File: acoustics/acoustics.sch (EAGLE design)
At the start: 172 parts, among them J1 22-27-2021-02, J2 22-27-2021-02, J3 22-27-2021-02, J4 22-27-2021-02, X1 22-23-2021, X2 22-23-2021, X3 22-23-2021, X4 22-23-2021

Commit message: One channel done-ish for 4/5 meeting with Dave
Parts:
- removed C15, C16, C17, C19, C20, C21, C49: 1uf, rcl:C-EUC0805K
- removed C50: 10uf, rcl:C-EUC0805K
- removed C51: 0.1uf, rcl:C-EUC0805K
- removed C52: 47uf, rcl:C-EUC0805K
- removed R5: 60.4k, rcl:R-US_M0805
- removed R6: 10K, rcl:R-US_M0805
- added H4ADC_C: 1uf, rcl:C-EUC0603K
- added H4RF_C_4, H4_C1, H4_C11, H4_C2, H4_C25, H4_C_POW: 1uf, rcl:C-EUC0603
- added H4RF_C_IN: 10uf, rcl:C-EUC0603
- added H4RF_C_O1: 47uf, rcl:C-EUC0603
- added H4RF_C_O2: 0.1uf, rcl:C-EUC0603
- added H4_R6: 10K, rcl:R-US_R0603
- added H4_R7: 60.4k, rcl:R-US_R0603
- renumbered C63 to HFPA_C, C64 to HFPA_C_INP, C65 to HFPA_C_FB, C66 to H4PA_C_IN, C67 to H4DA_C_OFN, C68 to H4DA_C_OFP, C69 to H4DA_CI2, C70 to H4DA_CI1, C72 to H4DA_C_O, J1 to H1CON, J2 to H2CON, J3 to H3CON, J4 to H4_OUT, R49 to HFPA_R_FB, R50 to HFPA_R, R51 to HFPA_R2, R52 to HFPA_R_IN, R53 to H4DA_R_IP2, R54 to H4DA_R_IP1, R55 to H4DA_R_IN1, R56 to H4DA_R_IN2, R57 to H4DA_R_ON1, R58 to H4DA_R_OP1, R59 to H4DA_R_OFN, R60 to H4DA_R_OFP, R63 to H4DA_R_ON2, R64 to H4DA_R_OP2, R69 to H4RF_R_3, R70 to H4RF_R_0, U$12 to H4_REFGEN, U$8 to H4_DIFAMP, U$9 to H4_PREAMP, X4 to H4_IN
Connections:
- net N$6 renamed START
- new net H4_REFV: ADC_H4.REFP, H4RF_C_O1.2, H4RF_C_O2.2, H4_REFGEN.OUT_F, H4_REFGEN.OUT_S
- net +3V3: now also H4ADC_C.1, H4RF_C_IN.2, H4_C_POW.1; no longer C17.1, C20.1, C50.2
- net AGND: now also H4ADC_C.2, H4RF_C_4.1, H4RF_C_IN.1, H4RF_C_O2.1, H4_C1.1, H4_C11.2, H4_C2.1, H4_R6.2, H4_R7.2; no longer C15.1, C16.1, C17.2, C19.2, C49.1, C50.1, C51.1, R5.2, R6.2
- net GND: now also ADC_H4.FILTER0, ADC_H4.FILTER1, ADC_H4.FSMODE, H4_C25.1, H4_C_POW.2; no longer C20.2, C21.1
- net N$11: now also H4_C1.2; no longer C16.2
- net N$24: now also H4_C2.2; no longer C15.2
- net N$31: now also H4_R6.1; no longer R6.1
- net N$32: now also H4_R7.1; no longer R5.1
- net N$35: now also H4_C11.1; no longer C19.1
- net N$38: now also H4_C25.2; no longer C21.2
- net N$83: now also H4RF_C_4.2; no longer C49.2
- net N$85: now also H4RF_C_O1.1; no longer C52.1
- net POSITIVE_REF: no longer ADC_H4.REFP, C51.2, C52.2, H4_REFGEN.OUT_F, H4_REFGEN.OUT_S

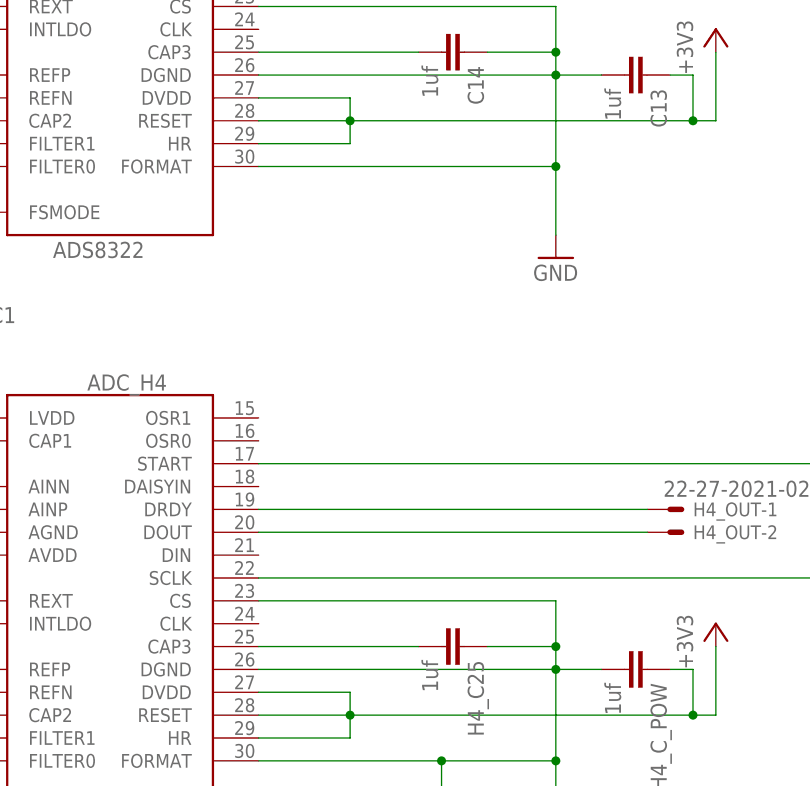
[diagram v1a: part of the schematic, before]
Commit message: One channel done updated Dave's suggestions
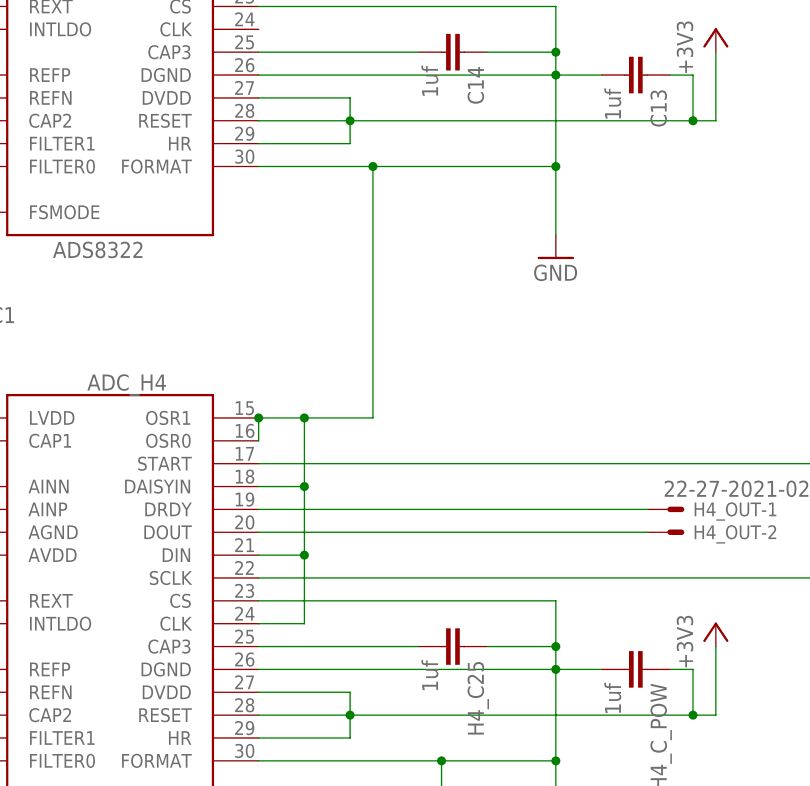
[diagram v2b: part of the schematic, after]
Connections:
- net GND: now also ADC_H4.CLK, ADC_H4.DAISYIN, ADC_H4.DIN, ADC_H4.OSR0, ADC_H4.OSR1
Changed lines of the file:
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@@
 <wire x1="269.24" y1="-71.12" x2="269.24" y2="-81.28" width="0.1524" layer="91"/>
 <wire x1="269.24" y1="-81.28" x2="269.24" y2="-88.9" width="0.1524" layer="91"/>
-<wire x1="236.22" y1="-81.28" x2="269.24" y2="-81.28" width="0.1524" layer="91"/>
+<wire x1="236.22" y1="-81.28" x2="248.92" y2="-81.28" width="0.1524" layer="91"/>
 <junction x="269.24" y="-81.28"/>
 <pinref part="GND2" gate="1" pin="GND"/>
 <pinref part="C14" gate="G$1" pin="1"/>
+<wire x1="248.92" y1="-81.28" x2="269.24" y2="-81.28" width="0.1524" layer="91"/>
 <wire x1="261.62" y1="-68.58" x2="269.24" y2="-68.58" width="0.1524" layer="91"/>
 <junction x="269.24" y="-68.58"/>
@@
 <pinref part="C13" gate="G$1" pin="2"/>
 <wire x1="274.32" y1="-71.12" x2="269.24" y2="-71.12" width="0.1524" layer="91"/>
+<pinref part="ADC_H4" gate="G$1" pin="OSR1"/>
+<pinref part="ADC_H4" gate="G$1" pin="OSR0"/>
+<wire x1="236.22" y1="-109.22" x2="236.22" y2="-111.76" width="0.1524" layer="91"/>
+<wire x1="236.22" y1="-109.22" x2="241.3" y2="-109.22" width="0.1524" layer="91"/>
+<wire x1="241.3" y1="-109.22" x2="248.92" y2="-109.22" width="0.1524" layer="91"/>
+<wire x1="248.92" y1="-109.22" x2="248.92" y2="-81.28" width="0.1524" layer="91"/>
+<junction x="236.22" y="-109.22"/>
+<junction x="248.92" y="-81.28"/>
+<pinref part="ADC_H4" gate="G$1" pin="DAISYIN"/>
+<wire x1="236.22" y1="-116.84" x2="241.3" y2="-116.84" width="0.1524" layer="91"/>
+<wire x1="241.3" y1="-116.84" x2="241.3" y2="-109.22" width="0.1524" layer="91"/>
+<junction x="241.3" y="-109.22"/>
+<pinref part="ADC_H4" gate="G$1" pin="DIN"/>
+<wire x1="236.22" y1="-124.46" x2="241.3" y2="-124.46" width="0.1524" layer="91"/>
+<wire x1="241.3" y1="-124.46" x2="241.3" y2="-116.84" width="0.1524" layer="91"/>
+<junction x="241.3" y="-116.84"/>
+<pinref part="ADC_H4" gate="G$1" pin="CLK"/>
+<wire x1="236.22" y1="-132.08" x2="241.3" y2="-132.08" width="0.1524" layer="91"/>
+<wire x1="241.3" y1="-132.08" x2="241.3" y2="-124.46" width="0.1524" layer="91"/>
+<junction x="241.3" y="-124.46"/>
 </segment>
 </net>

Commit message: Combining AGND and GND into one
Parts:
- removed C1, C10, C11, C12, C13, C14, C2, C3, C4, C47, C5, C6, C7, C9: 1uf, rcl:C-EUC0805K
- removed C48, C8: 10uf, rcl:C-EUC0805K
- removed C74, C76: 0.1uf, rcl:C-EUC0805K
- removed C75, C77: 47uf, rcl:C-EUC0805K
- removed R1, R2: 60.4k, rcl:R-US_M0805
- removed R3, R4: 10K, rcl:R-US_M0805
- added H2ADC_C9, H3ADC_C9: 0.1uf, rcl:C-EUC0603
- added H2RF_C1, H3RF_C1: 10uf, rcl:C-EUC0603
- added H2RF_C4, H2_C1, H2_C11, H2_C2, H2_C25, H2_C27, H2_C6, H3RF_C4, H3_ADC_C5, H3_C1, H3_C11, H3_C2, H3_C25, H3_C27: 1uf, rcl:C-EUC0603
- added H2RF_C6, H3RF_C6: 47uf, rcl:C-EUC0603
- added H2_R7, H3_R7: 60.4k, rcl:R-US_R0603
- added H2_R8, H3_R8: 10K, rcl:R-US_R0603
- renumbered R67 to H2RF_R3, R68 to H3RF_R3, R71 to H2RF_RO, R72 to H3RF_RO
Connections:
- new net N$37: ADC_H3.REFP, H3ADC_C9.2, H3RF_C6.2, U$11.OUT_F, U$11.OUT_S
- new net N$6: ADC_H1.REFP, C25.2, C73.2, U$1.OUT_F, U$1.OUT_S
- net +3V3: now also H2RF_C1.2, H2_C27.1, H2_C6.2, H3RF_C1.2, H3_ADC_C5.1, H3_C27.1; no longer C10.1, C11.2, C12.1, C13.1, C48.2, C8.2
- net AGND: no longer ADC_H1.AGND, ADC_H1.REFN, ADC_H2.AGND, ADC_H2.REFN, ADC_H3.AGND, ADC_H3.REFN, ADC_H4.AGND, ADC_H4.REFN, C1.1, C10.2, C11.1, C2.1, C22.1, C23.1, C24.2, C25.1, C26.2, C29.1, C3.1, C30.1, C31.1, C39.1, C4.2, C41.2, C47.1, C48.1, C54.1, C55.2, C6.1, C7.1, C74.1, C76.1, C8.1, C9.2, H2RF_R3.1, H2RF_RO.1, H3RF_R3.1, H3RF_RO.1, H4ADC_C.2, H4DA_R_IN1.1, H4RF_C_4.1, H4RF_C_IN.1, H4RF_C_O2.1, H4RF_R_0.1, H4RF_R_3.1, H4_C1.1, H4_C11.2, H4_C2.1, H4_DIFAMP.VS-, H4_IN-1.S, H4_PREAMP.V-, H4_R6.2, H4_R7.2, H4_REFGEN.GND_F, H4_REFGEN.GND_S, HFPA_C.1, HFPA_C_INP.2, HFPA_R.2, R1.2, R15.1, R2.2, R24.2, R29.1, R3.2, R36.2, R4.2, R41.1, R65.1, R66.1, R7.2, R8.2, U$1.GND_F, U$1.GND_S, U$10.GND_F, U$10.GND_S, U$11.GND_F, U$11.GND_S, U$2.VS-, U$3.VS-, U$4.V-, U$5.VS-, U$6.V-, U$7.V-, X1-1.S, X2-1.S, X3-1.S
- net GND: now also ADC_H1.AGND, ADC_H1.REFN, ADC_H2.AGND, ADC_H2.DAISYIN, ADC_H2.DIN, ADC_H2.FILTER0, ADC_H2.FILTER1, ADC_H2.FSMODE, ADC_H2.OSR0, ADC_H2.OSR1, ADC_H2.REFN, ADC_H3.AGND, ADC_H3.DAISYIN, ADC_H3.DIN, ADC_H3.FILTER0, ADC_H3.FILTER1, ADC_H3.FSMODE, ADC_H3.OSR0, ADC_H3.OSR1, ADC_H3.REFN, ADC_H4.AGND, ADC_H4.REFN, C22.1, C23.1, C24.2, C25.1, C26.2, C29.1, C30.1, C31.1, C39.1, C41.2, C54.1, C55.2, H2ADC_C9.1, H2RF_C1.1, H2RF_C4.1, H2RF_R3.1, H2RF_RO.1, H2_C1.1, H2_C11.2, H2_C2.1, H2_C25.1, H2_C27.2, H2_C6.1, H2_R7.2, H2_R8.2, H3ADC_C9.1, H3RF_C1.1, H3RF_C4.1, H3RF_R3.1, H3RF_RO.1, H3_ADC_C5.2, H3_C1.1, H3_C11.2, H3_C2.1, H3_C25.1, H3_C27.2, H3_R7.2, H3_R8.2, H4ADC_C.2, H4DA_R_IN1.1, H4RF_C_4.1, H4RF_C_IN.1, H4RF_C_O2.1, H4RF_R_0.1, H4RF_R_3.1, H4_C1.1, H4_C11.2, H4_C2.1, H4_DIFAMP.VS-, H4_IN-1.S, H4_PREAMP.V-, H4_R6.2, H4_R7.2, H4_REFGEN.GND_F, H4_REFGEN.GND_S, HFPA_C.1, HFPA_C_INP.2, HFPA_R.2, R15.1, R24.2, R29.1, R36.2, R41.1, R65.1, R66.1, R7.2, R8.2, U$1.GND_F, U$1.GND_S, U$10.GND_F, U$10.GND_S, U$11.GND_F, U$11.GND_S, U$2.VS-, U$3.VS-, U$4.V-, U$5.VS-, U$6.V-, U$7.V-, X1-1.S, X2-1.S, X3-1.S; no longer ADC_H4.CLK, C12.2, C13.2, C14.1, C5.1
- net N$1: now also H2_C1.2; no longer C2.2
- net N$12: now also H3_C1.2; no longer C7.2
- net N$13: now also H2_C25.2; no longer C5.2
- net N$18: now also H3_R7.1; no longer R2.1
- net N$21: now also H3_C11.1; no longer C9.1
- net N$22: now also H2_R8.1; no longer R3.1
- net N$23: now also H3_R8.1; no longer R4.1
- net N$3: now also H2_C2.2; no longer C1.2
- net N$30: now also H3_C25.2; no longer C14.2
- net N$4: now also H2_R7.1; no longer R1.1
- net N$42: now also H2RF_C4.2; no longer C3.2
- net N$47: now also H3RF_C4.2; no longer C47.2
- net N$8: now also H3_C2.2; no longer C6.2
- net N$86: now also H2RF_C6.1; no longer C75.1
- net N$87: now also H3RF_C6.1; no longer C77.1
- net N$9: now also H2_C11.1; no longer C4.1
- net POSITIVE_REF: now also H2ADC_C9.2, H2RF_C6.2; no longer ADC_H1.REFP, ADC_H3.REFP, C25.2, C73.2, C74.2, C75.2, C76.2, C77.2, U$1.OUT_F, U$1.OUT_S, U$11.OUT_F, U$11.OUT_S

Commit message: Initial placement of parts completed
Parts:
- removed C22, C23, C24, C26, C27, C28, C29: 1uf, rcl:C-EUC0805K
- removed C25: 0.1uf, rcl:C-EUC0805K
- removed C30: 10uf, rcl:C-EUC0805K
- removed C73: 47uf, rcl:C-EUC0805K
- removed R16, R30, R42: 330, resistor:R-US_R0603
- removed R7: 60.4k, rcl:R-US_M0805
- removed R8: 10K, rcl:R-US_M0805
- added H1ADC_C1, H1ADC_C11, H1ADC_C2, H1ADC_C25, H1ADC_C27, H1ADC_C6, H1RF_C4: 1uf, rcl:C-EUC0603
- added H1ADC_C9: 0.1uf, rcl:C-EUC0603
- added H1ADC_R7: 60.4k, rcl:R-US_R0603
- added H1ADC_R8: 10K, rcl:R-US_R0603
- added H1DA_R_IN2, H2DA_R_IN2, H3DA_R_IN2: 330, resistor:R-US_R0603
- added H1RF_C1: 10uf, rcl:C-EUC0603
- added H1RF_C6: 47uf, rcl:C-EUC0603
- renumbered C31 to H1PA_C, C32 to H1DA_C_OFN, C33 to H1PA_C_INP, C34 to H1PA_C_FB, C35 to H1PA_C_IN, C36 to H1DA_C_OFP, C37 to H1DA_C_I2, C38 to H1DA_C_I1, C39 to H2PA_C, C40 to H1DA_CO, C41 to H2PA_C_INP, C42 to H2PA_C_FB, C43 to H2PA_C_IN, C44 to H2DA_C_OFN, C45 to H2DA_C_OFP, C46 to H2DA_C_I2, C53 to H2DA_C_I1, C54 to H3PA_C, C55 to H3PA_C_INP, C56 to H3PA_C_FB, C57 to H3PA_C_IN, C58 to H3DA_C_OFN, C59 to H3DA_C_OFP, C60 to H3DA_C_I2, C61 to H3DA_C_I1, C62 to H2DA_CO, C71 to H3DA_CO, R10 to H1DA_R_IP2, R11 to H1PA_R, R12 to H1PA_R2, R13 to H1PA_R_IN, R14 to H1DA_R_IP1, R15 to H1DA_R_IN1, R17 to H1DA_R_ON1, R18 to H1DA_R_ON2, R19 to H1DA_R_OP1, R20 to H1DA_R_OP2, R21 to H1DA_R_OFN, R22 to H1DA_R_OFP, R23 to H2PA_R_FB, R24 to H2PA_R, R25 to H2PA_R2, R26 to H2PA_R_IN, R27 to H2DA_R_IP2, R28 to H2DA_R_IP1, R29 to H2DA_R_IN1, R31 to H2DA_R_ON1, R32 to H2DA_R_OP1, R33 to H2DA_R_OFN, R34 to H2DA_R_OFP, R35 to H3PA_R_FB, R36 to H3PA_R, R37 to H3PA_R2, R38 to H3PA_R_IN, R39 to H3DA_R_IP2, R40 to H3DA_R_IP1, R41 to H3DA_R_IN1, R43 to H3DA_R_ON1, R44 to H3DA_R_OP1, R45 to H3DA_R_OFN, R46 to H3DA_R_OFP, R47 to H2DA_R_ON2, R48 to H2DA_R_OP2, R61 to H3DA_R_ON2, R62 to H3DA_R__OP2, R65 to H1RF_R3, R66 to H1RF_RO, R9 to H1PA_R_FB, U$2 to H1DA, U$3 to H2DA, U$4 to H2PA, U$5 to H3DA, U$6 to H1PA, U$7 to H3PA, X1 to H1_IN, X2 to H2_IN, X3 to H3_IN
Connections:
- removed net AGND: H1PA_C_INP.2, H1PA_R.2
- new net CLK: ADC_H1.CLK, ADC_H2.CLK, ADC_H3.CLK, ADC_H4.CLK
- net +3V3: now also H1ADC_C27.1, H1ADC_C6.1, H1RF_C1.2; no longer C24.1, C27.1, C30.2
- net GND: now also ADC_H1.DAISYIN, ADC_H1.DIN, ADC_H1.FILTER0, ADC_H1.FILTER1, ADC_H1.FSMODE, ADC_H1.OSR0, ADC_H1.OSR1, H1ADC_C1.1, H1ADC_C11.2, H1ADC_C2.1, H1ADC_C25.1, H1ADC_C27.2, H1ADC_C6.2, H1ADC_C9.1, H1ADC_R7.2, H1ADC_R8.2, H1PA_C_INP.2, H1PA_R.2, H1RF_C1.1, H1RF_C4.1; no longer C22.1, C23.1, C24.2, C25.1, C26.2, C27.2, C28.1, C29.1, C30.1, R7.2, R8.2
- net N$17: now also H1DA_C_I2.2, H1DA_R_IN2.2; no longer R16.2
- net N$2: now also H1RF_C4.2; no longer C29.2
- net N$25: now also H1DA_R_IN2.1; no longer R16.1
- net N$39: now also H1ADC_C1.2; no longer C23.2
- net N$40: now also H1ADC_C2.2; no longer C22.2
- net N$44: now also H1ADC_R7.1; no longer R7.1
- net N$45: now also H1ADC_R8.1; no longer R8.1
- net N$46: now also H1RF_C6.1; no longer C73.1
- net N$48: now also H1ADC_C11.1; no longer C26.1
- net N$50: now also H2DA_C_I2.2, H2DA_R_IN2.2; no longer R30.2
- net N$52: now also H2DA_R_IN2.1; no longer R30.1
- net N$56: now also H1ADC_C25.2; no longer C28.2
- net N$6: now also H1ADC_C9.2, H1RF_C6.2; no longer C25.2, C73.2
- net N$63: now also H3DA_C_I2.2, H3DA_R_IN2.2; no longer R42.2
- net N$65: now also H3DA_R_IN2.1; no longer R42.1

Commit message: Fixing connector placement of signal connectors
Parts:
- added DCON: 22-27-2021-02, con-molex:22-27-2021-02
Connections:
- net SCLK: now also DCON-2.S
- net START: now also DCON-1.S
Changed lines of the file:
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@@
 <grid distance="0.1" unitdist="inch" unit="inch" style="lines" multiple="1" display="no" altdistance="0.01" altunitdist="inch" altunit="inch"/>
 <layers>
-<layer number="1" name="Top" color="4" fill="1" visible="yes" active="no"/>
-<layer number="2" name="Route2" color="1" fill="1" visible="yes" active="no"/>
-<layer number="3" name="Route3" color="4" fill="3" visible="yes" active="no"/>
-<layer number="4" name="Route4" color="1" fill="4" visible="yes" active="no"/>
-<layer number="5" name="Route5" color="4" fill="4" visible="yes" active="no"/>
-<layer number="6" name="Route6" color="1" fill="8" visible="yes" active="no"/>
-<layer number="7" name="Route7" color="4" fill="8" visible="yes" active="no"/>
-<layer number="8" name="Route8" color="1" fill="2" visible="yes" active="no"/>
-<layer number="9" name="Route9" color="4" fill="2" visible="yes" active="no"/>
-<layer number="10" name="Route10" color="1" fill="7" visible="yes" active="no"/>
-<layer number="11" name="Route11" color="4" fill="7" visible="yes" active="no"/>
-<layer number="12" name="Route12" color="1" fill="5" visible="yes" active="no"/>
-<layer number="13" name="Route13" color="4" fill="5" visible="yes" active="no"/>
-<layer number="14" name="Route14" color="1" fill="6" visible="yes" active="no"/>
-<layer number="15" name="Route15" color="14" fill="1" visible="yes" active="no"/>
-<layer number="16" name="Bottom" color="13" fill="1" visible="yes" active="no"/>
-<layer number="17" name="Pads" color="2" fill="1" visible="yes" active="no"/>
-<layer number="18" name="Vias" color="2" fill="1" visible="yes" active="no"/>
-<layer number="19" name="Unrouted" color="6" fill="1" visible="yes" active="no"/>
-<layer number="20" name="Dimension" color="24" fill="1" visible="yes" active="no"/>
-<layer number="21" name="tPlace" color="7" fill="1" visible="yes" active="no"/>
-<layer number="22" name="bPlace" color="7" fill="1" visible="yes" active="no"/>
-<layer number="23" name="tOrigins" color="15" fill="1" visible="yes" active="no"/>
-<layer number="24" name="bOrigins" color="15" fill="1" visible="yes" active="no"/>
-<layer number="25" name="tNames" color="7" fill="1" visible="yes" active="no"/>
-<layer number="26" name="bNames" color="7" fill="1" visible="yes" active="no"/>
-<layer number="27" name="tValues" color="7" fill="1" visible="yes" active="no"/>
-<layer number="28" name="bValues" color="7" fill="1" visible="yes" active="no"/>
+<layer number="1" name="Top" color="4" fill="1" visible="no" active="no"/>
+<layer number="2" name="Route2" color="1" fill="1" visible="no" active="no"/>
+<layer number="3" name="Route3" color="4" fill="3" visible="no" active="no"/>
+<layer number="4" name="Route4" color="1" fill="4" visible="no" active="no"/>
+<layer number="5" name="Route5" color="4" fill="4" visible="no" active="no"/>
+<layer number="6" name="Route6" color="1" fill="8" visible="no" active="no"/>
+<layer number="7" name="Route7" color="4" fill="8" visible="no" active="no"/>
+<layer number="8" name="Route8" color="1" fill="2" visible="no" active="no"/>
+<layer number="9" name="Route9" color="4" fill="2" visible="no" active="no"/>
+<layer number="10" name="Route10" color="1" fill="7" visible="no" active="no"/>
+<layer number="11" name="Route11" color="4" fill="7" visible="no" active="no"/>
+<layer number="12" name="Route12" color="1" fill="5" visible="no" active="no"/>
+<layer number="13" name="Route13" color="4" fill="5" visible="no" active="no"/>
+<layer number="14" name="Route14" color="1" fill="6" visible="no" active="no"/>
+<layer number="15" name="Route15" color="14" fill="1" visible="no" active="no"/>
+<layer number="16" name="Bottom" color="13" fill="1" visible="no" active="no"/>
+<layer number="17" name="Pads" color="2" fill="1" visible="no" active="no"/>
+<layer number="18" name="Vias" color="2" fill="1" visible="no" active="no"/>
+<layer number="19" name="Unrouted" color="6" fill="1" visible="no" active="no"/>
+<layer number="20" name="Dimension" color="24" fill="1" visible="no" active="no"/>
+<layer number="21" name="tPlace" color="7" fill="1" visible="no" active="no"/>
+<layer number="22" name="bPlace" color="7" fill="1" visible="no" active="no"/>
+<layer number="23" name="tOrigins" color="15" fill="1" visible="no" active="no"/>
+<layer number="24" name="bOrigins" color="15" fill="1" visible="no" active="no"/>
+<layer number="25" name="tNames" color="7" fill="1" visible="no" active="no"/>
+<layer number="26" name="bNames" color="7" fill="1" visible="no" active="no"/>
+<layer number="27" name="tValues" color="7" fill="1" visible="no" active="no"/>
+<layer number="28" name="bValues" color="7" fill="1" visible="no" active="no"/>
 <layer number="29" name="tStop" color="7" fill="3" visible="no" active="no"/>
 <layer number="30" name="bStop" color="7" fill="6" visible="no" active="no"/>
@@
 <layer number="35" name="tGlue" color="7" fill="4" visible="no" active="no"/>
 <layer number="36" name="bGlue" color="7" fill="5" visible="no" active="no"/>
-<layer number="37" name="tTest" color="7" fill="1" visible="yes" active="no"/>
-<layer number="38" name="bTest" color="7" fill="1" visible="yes" active="no"/>
+<layer number="37" name="tTest" color="7" fill="1" visible="no" active="no"/>
+<layer number="38" name="bTest" color="7" fill="1" visible="no" active="no"/>
 <layer number="39" name="tKeepout" color="4" fill="11" visible="no" active="no"/>
 <layer number="40" name="bKeepout" color="1" fill="11" visible="no" active="no"/>
@@
 <layer number="44" name="Drills" color="7" fill="1" visible="no" active="no"/>
 <layer number="45" name="Holes" color="7" fill="1" visible="no" active="no"/>
-<layer number="46" name="Milling" color="3" fill="1" visible="yes" active="no"/>
-<layer number="47" name="Measures" color="7" fill="1" visible="yes" active="no"/>
-<layer number="48" name="Document" color="7" fill="1" visible="yes" active="no"/>
-<layer number="49" name="Reference" color="7" fill="1" visible="yes" active="no"/>
-<layer number="50" name="dxf" color="7" fill="1" visible="yes" active="no"/>
-<layer number="51" name="tDocu" color="7" fill="1" visible="yes" active="no"/>
-<layer number="52" name="bDocu" color="7" fill="1" visible="yes" active="no"/>
-<layer number="53" name="tGND_GNDA" color="7" fill="9" visible="yes" active="no"/>
-<layer number="54" name="bGND_GNDA" color="1" fill="9" visible="yes" active="no"/>
-<layer number="56" name="wert" color="7" fill="1" visible="yes" active="no"/>
-<layer number="57" name="tCAD" color="7" fill="1" visible="yes" active="no"/>
-<layer number="59" name="tCarbon" color="7" fill="1" visible="yes" active="no"/>
-<layer number="60" name="bCarbon" color="7" fill="1" visible="yes" active="no"/>
+<layer number="46" name="Milling" color="3" fill="1" visible="no" active="no"/>
+<layer number="47" name="Measures" color="7" fill="1" visible="no" active="no"/>
+<layer number="48" name="Document" color="7" fill="1" visible="no" active="no"/>
+<layer number="49" name="Reference" color="7" fill="1" visible="no" active="no"/>
+<layer number="50" name="dxf" color="7" fill="1" visible="no" active="no"/>
+<layer number="51" name="tDocu" color="7" fill="1" visible="no" active="no"/>
+<layer number="52" name="bDocu" color="7" fill="1" visible="no" active="no"/>
+<layer number="53" name="tGND_GNDA" color="7" fill="9" visible="no" active="no"/>
+<layer number="54" name="bGND_GNDA" color="1" fill="9" visible="no" active="no"/>
+<layer number="56" name="wert" color="7" fill="1" visible="no" active="no"/>
+<layer number="57" name="tCAD" color="7" fill="1" visible="no" active="no"/>
+<layer number="59" name="tCarbon" color="7" fill="1" visible="no" active="no"/>
+<layer number="60" name="bCarbon" color="7" fill="1" visible="no" active="no"/>
 <layer number="88" name="SimResults" color="9" fill="1" visible="yes" active="yes"/>
 <layer number="89" name="SimProbes" color="9" fill="1" visible="yes" active="yes"/>
@@
 <part name="H3RF_C6" library="rcl" library_urn="urn:adsk.eagle:library:334" deviceset="C-EU" device="C0603" package3d_urn="urn:adsk.eagle:package:23616/2" value="47uf"/>
 <part name="H4_DIFAMP" library="THS4551" deviceset="THS4551" device=""/>
+<part name="DCON" library="con-molex" library_urn="urn:adsk.eagle:library:165" deviceset="22-?-02" device="27-2021"/>
 </parts>
 <sheets>
@@
 <instance part="H3RF_C6" gate="G$1" x="144.78" y="-73.66" rot="R180"/>
 <instance part="H4_DIFAMP" gate="G$1" x="30.48" y="-119.38"/>
+<instance part="DCON" gate="-1" x="337.82" y="33.02"/>
+<instance part="DCON" gate="-2" x="337.82" y="27.94"/>
 </instances>
 <busses>
@@
 <pinref part="ADC_H1" gate="G$1" pin="START"/>
 <wire x1="236.22" y1="73.66" x2="299.72" y2="73.66" width="0.1524" layer="91"/>
-<wire x1="299.72" y1="73.66" x2="299.72" y2="15.24" width="0.1524" layer="91"/>
+<wire x1="299.72" y1="73.66" x2="299.72" y2="33.02" width="0.1524" layer="91"/>
 <junction x="299.72" y="15.24"/>
+<pinref part="DCON" gate="-1" pin="S"/>
+<wire x1="299.72" y1="33.02" x2="299.72" y2="15.24" width="0.1524" layer="91"/>
+<wire x1="335.28" y1="33.02" x2="299.72" y2="33.02" width="0.1524" layer="91"/>
+<junction x="299.72" y="33.02"/>
 </segment>
 </net>
@@
 <pinref part="ADC_H1" gate="G$1" pin="SCLK"/>
 <wire x1="236.22" y1="60.96" x2="307.34" y2="60.96" width="0.1524" layer="91"/>
-<wire x1="307.34" y1="60.96" x2="307.34" y2="2.54" width="0.1524" layer="91"/>
+<wire x1="307.34" y1="60.96" x2="307.34" y2="27.94" width="0.1524" layer="91"/>
 <junction x="307.34" y="2.54"/>
-</segment>
-</net>
+<pinref part="DCON" gate="-2" pin="S"/>
+<wire x1="307.34" y1="27.94" x2="307.34" y2="2.54" width="0.1524" layer="91"/>
+<wire x1="335.28" y1="27.94" x2="307.34" y2="27.94" width="0.1524" layer="91"/>
+<junction x="307.34" y="27.94"/>
+</segment>
+</net>

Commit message: Adding power connection to acoustics
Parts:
- added U$2: 105313-1102, 105313-1102:105313-1102
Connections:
- net +3V3: now also U$2.P$1
- net GND: now also U$2.P$2
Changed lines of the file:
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@@
 <part name="H4_DIFAMP" library="THS4551" deviceset="THS4551" device=""/>
 <part name="DCON" library="con-molex" library_urn="urn:adsk.eagle:library:165" deviceset="22-?-02" device="27-2021"/>
+<part name="U$2" library="105313-1102" deviceset="105313-1102" device=""/>
+<part name="+3V21" library="supply1" library_urn="urn:adsk.eagle:library:371" deviceset="+3V3" device=""/>
+<part name="GND5" library="supply1" library_urn="urn:adsk.eagle:library:371" deviceset="GND" device=""/>
 </parts>
 <sheets>
@@
 <instance part="DCON" gate="-1" x="337.82" y="33.02"/>
 <instance part="DCON" gate="-2" x="337.82" y="27.94"/>
+<instance part="U$2" gate="G$1" x="335.28" y="-5.08"/>
+<instance part="+3V21" gate="G$1" x="325.12" y="5.08"/>
+<instance part="GND5" gate="1" x="325.12" y="-12.7"/>
 </instances>
 <busses>
@@
 <wire x1="60.96" y1="-137.16" x2="60.96" y2="-127" width="0.1524" layer="91"/>
 <junction x="60.96" y="-127"/>
+</segment>
+<segment>
+<pinref part="U$2" gate="G$1" pin="P$1"/>
+<pinref part="+3V21" gate="G$1" pin="+3V3"/>
+<wire x1="330.2" y1="-2.54" x2="325.12" y2="-2.54" width="0.1524" layer="91"/>
+<wire x1="325.12" y1="-2.54" x2="325.12" y2="2.54" width="0.1524" layer="91"/>
 </segment>
 </net>
@@
 <junction x="-86.36" y="55.88"/>
 </segment>
+<segment>
+<pinref part="U$2" gate="G$1" pin="P$2"/>
+<pinref part="GND5" gate="1" pin="GND"/>
+<wire x1="330.2" y1="-5.08" x2="325.12" y2="-5.08" width="0.1524" layer="91"/>
+<wire x1="325.12" y1="-5.08" x2="325.12" y2="-10.16" width="0.1524" layer="91"/>
+</segment>
 </net>
